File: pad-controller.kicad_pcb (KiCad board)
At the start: 2 copper layers, 86 x 64 mm, 50 parts, among them J4 Conn_01x02, J6 Conn_01x06, M1 Motor_Servo, M2 Motor_Servo, M3 Motor_Servo, M4 Motor_Servo, Q2 FQP30N06L, SW1 SW_Push_Dual, U1 Xbee, U2 TPS56121, U3 LD1117S33TR_SOT223

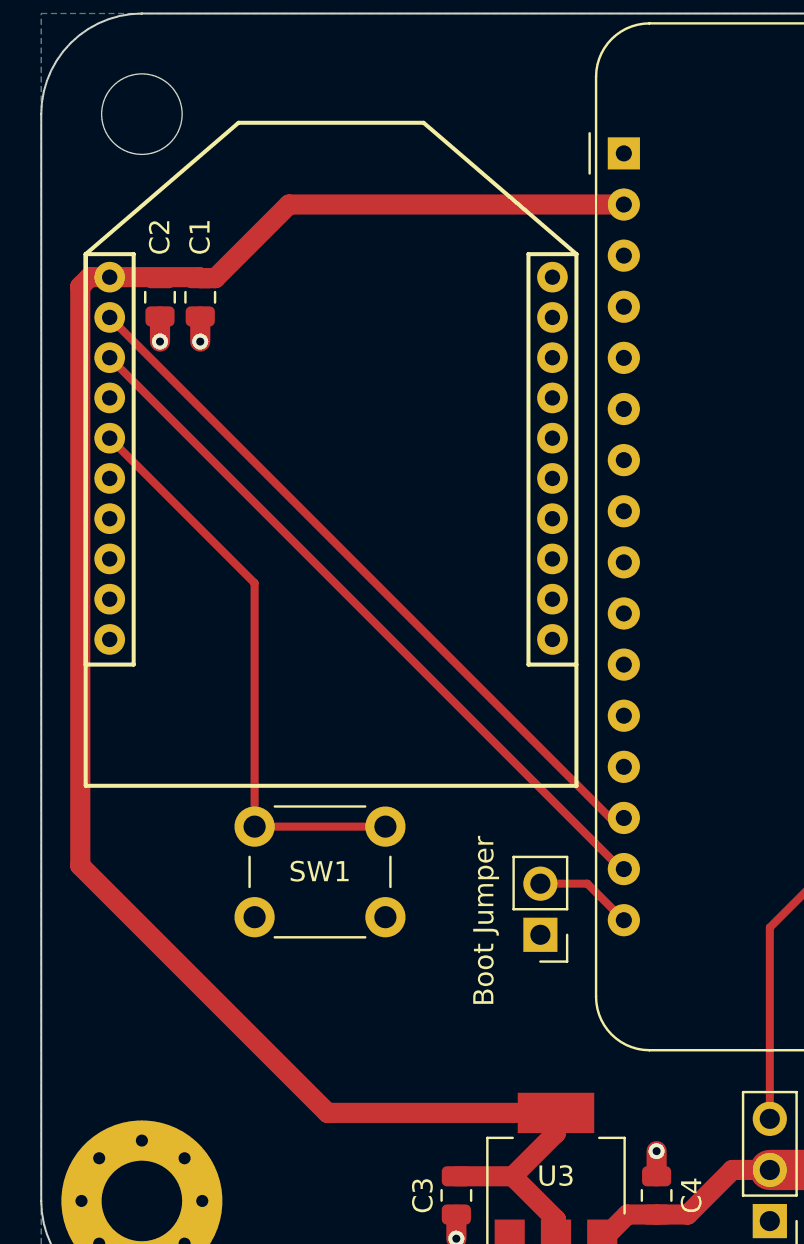
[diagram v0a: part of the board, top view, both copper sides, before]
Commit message: Add HSP logo and 3D model for wago terminal block
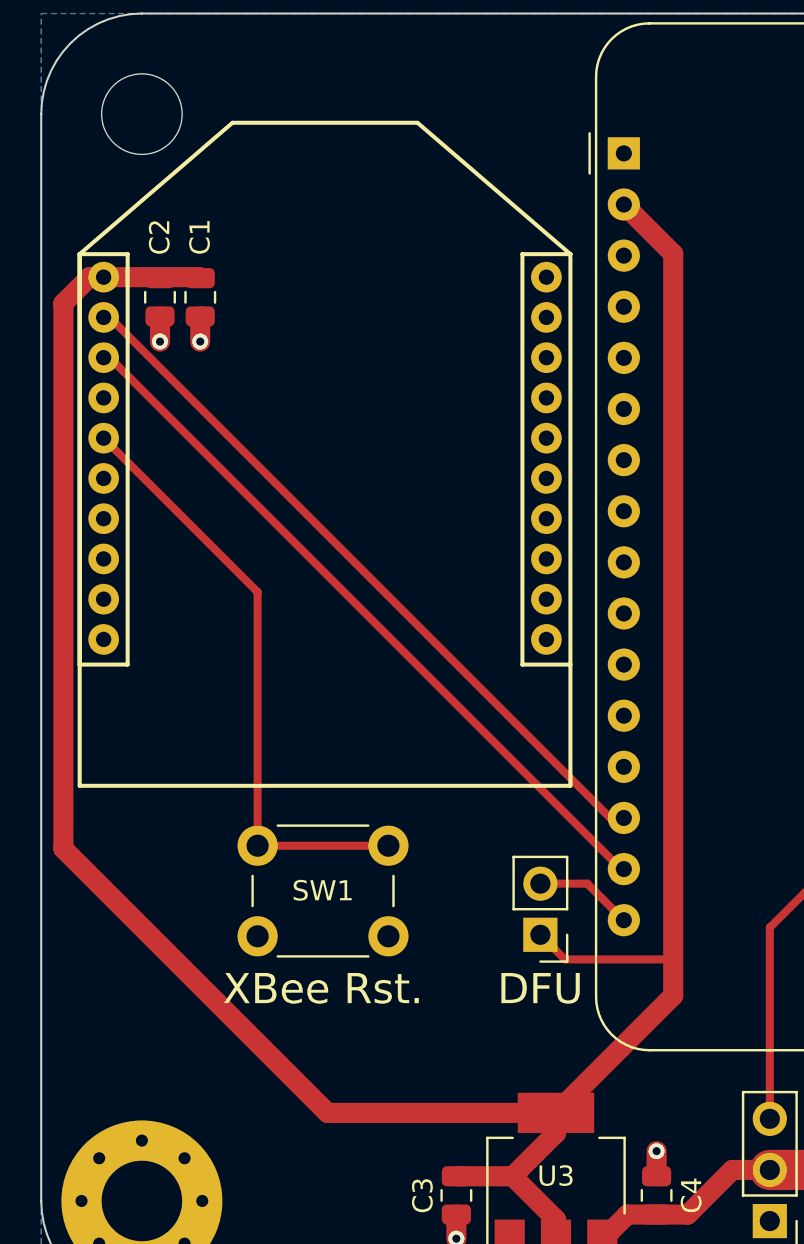
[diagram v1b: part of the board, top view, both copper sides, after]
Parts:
- added G***: LOGO, Logo Footprint Library:hsp-logo, B.Cu at (160.5, 70.7)
- J6: value Conn_01x06 -> Wago Terminal Block
- U1: value Xbee -> XBee
- moved SW1 0.96 mm to (110.8, 101.3)
- moved U1 0.30 mm to (114.1, 82.1)
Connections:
- JP1 pad 1: GND -> +3.3V
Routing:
- net +3.3V: track 97.1 -> 130.9 mm
- net /XBee Reset: track 28.8 -> 29.9 mm
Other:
- board text added: "DFU"
- board text added: "XBee Rst."

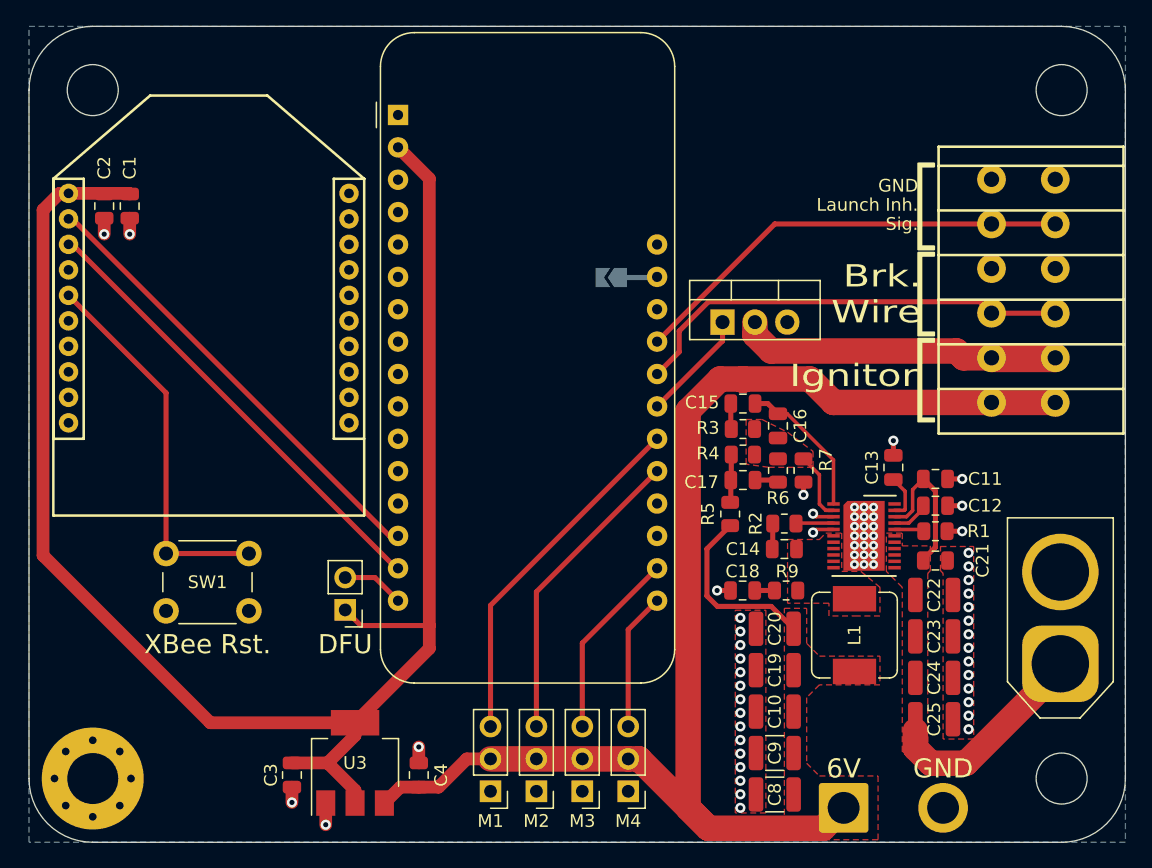
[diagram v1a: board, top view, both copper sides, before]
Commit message: Clean up schematic and board layout
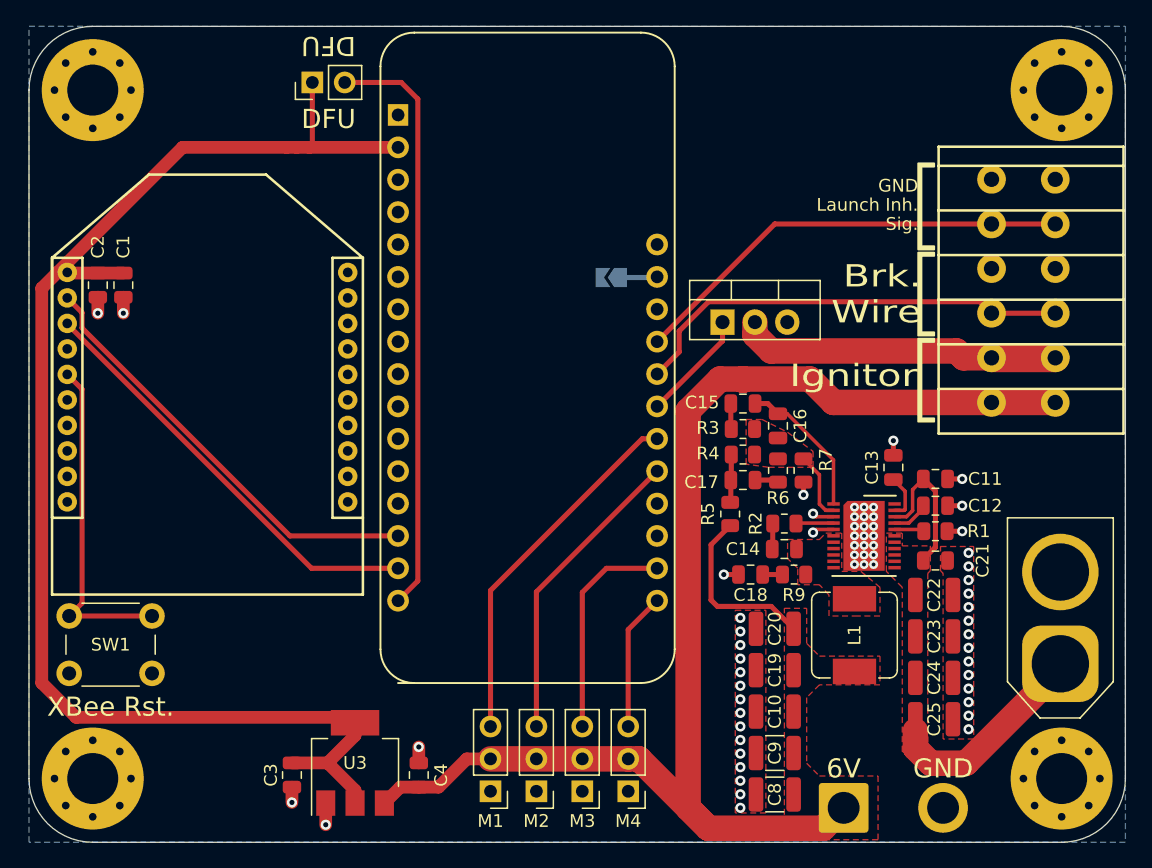
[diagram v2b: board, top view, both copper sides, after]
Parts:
- A1: footprint Module:Adafruit_Feather -> Marks_Footprints:Adafruit_Feather
- C15: value 390 pF -> 56 pF
- C16: value 12 pF -> 1.2 pF
- C17: value 820 pF -> 100 pF
- H1, H3, H4: value MountingHole -> MountingHole_Pad; footprint MountingHole:MountingHole_4mm -> MountingHole:MountingHole_4mm_Pad_Via
- R3: value 442 kΩ -> 390 kΩ
- R4: value 200 kΩ -> 20.5 kΩ
- R6: value 6200 Ω -> 5100 Ω
- R7: value 22 kΩ -> 2.2777778 kΩ
- moved JP1 41.5 mm to (122.2, 64.4), turned to 90 degrees
- moved SW1 9.04 mm to (103.2, 106.2)
- moved C1 6.22 mm to (107.4, 80.3)
- moved C2 6.22 mm to (105.4, 80.3)
- moved U1 6.20 mm to (114.0, 88.3)
- moved C18 1.40 mm to (156.6, 103.0)
- moved R9 1.40 mm to (160.0, 103.0)
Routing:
- net Net-(A1-SPARE): track 4.90 -> 46.3 mm
- net +3.3V: track 130.9 -> 110.6 mm
- net /XBee Reset: track 29.9 -> 26.4 mm
- net MCU TX: track 36.4 -> 33.9 mm
- net Servo 3 PWM: track 14.8 -> 17.2 mm
- net MCU RX: track 36.1 -> 34.4 mm
- net Servo 1 PWM: track 28.0 -> 28.7 mm

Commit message: Adjust back silkscreen
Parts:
- moved G*** 2.60 mm to (163.0, 70.0)
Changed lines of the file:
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@@
   )
   (footprint "Logo Footprint Library:hsp-logo" (layer "B.Cu")
-    (at 160.5 70.7 180)
+    (at 163 70 180)
     (attr board_only exclude_from_pos_files exclude_from_bom)
     (fp_text reference "G***" (at 0 0) (layer "B.SilkS") hide
@@
   )
   (gr_text_box "HSP Pad Controller v1.0"
-    (start 123.65 61.5) (end 156.35 65) (layer "B.SilkS")
+    (start 124.85 61.1) (end 157.55 64.6) (layer "B.SilkS")
       (effects (font (size 1.5 1.5) (thickness 0.25) bold) (justify left top mirror))
   )

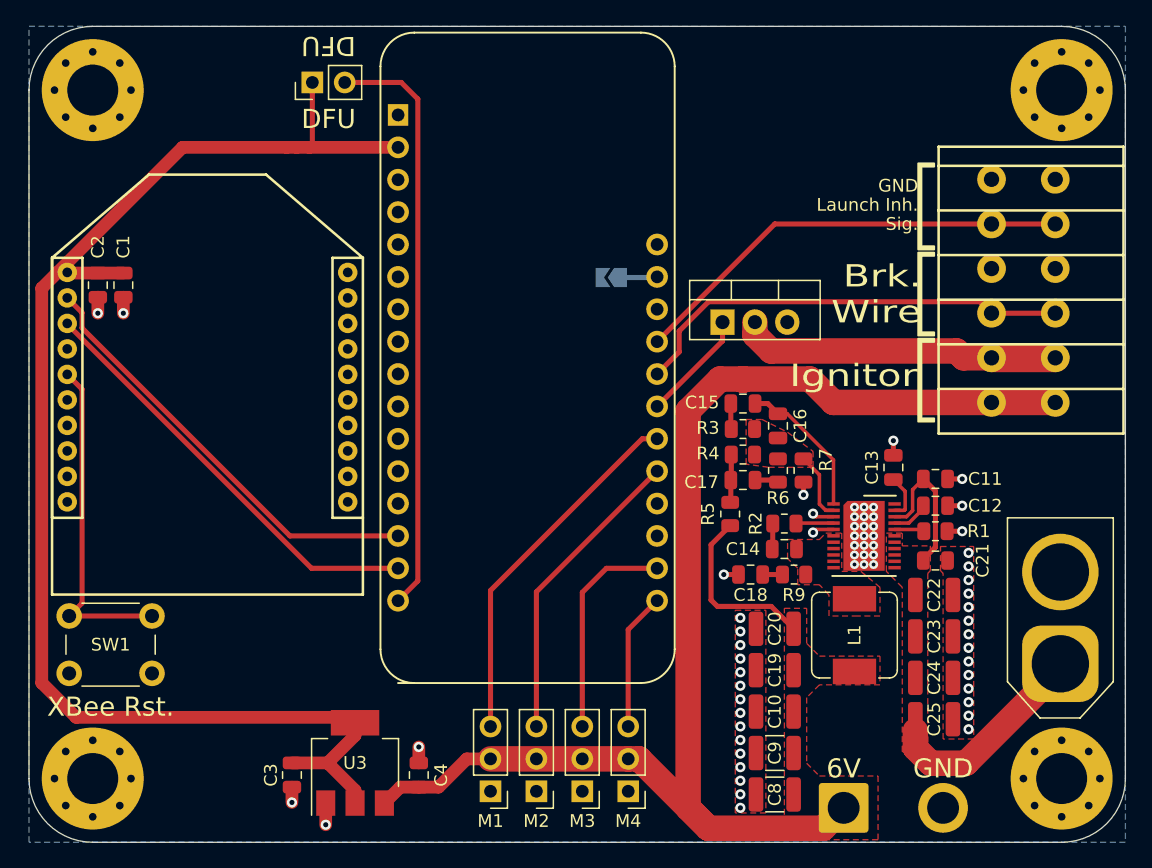
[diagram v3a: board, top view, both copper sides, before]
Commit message: Add silkscreen label for solder jumper
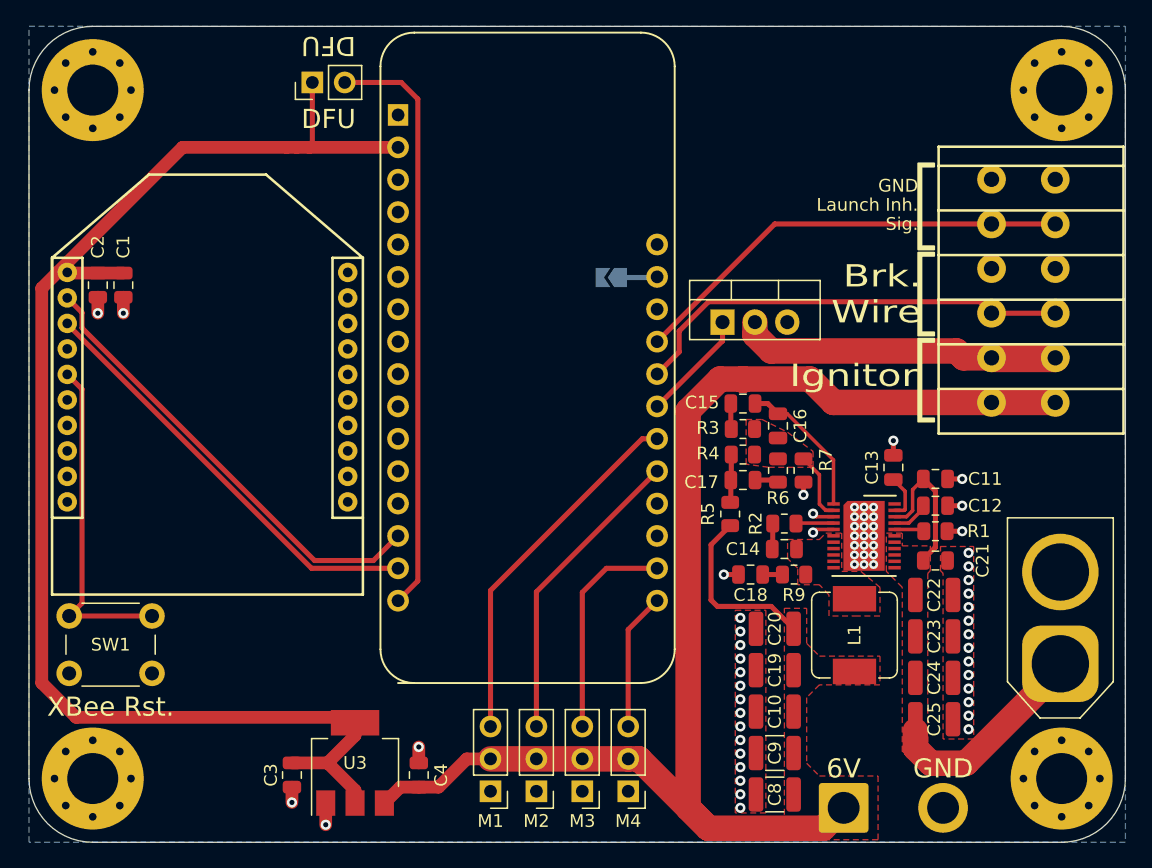
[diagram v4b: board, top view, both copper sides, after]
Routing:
- net MCU RX: track 34.4 -> 36.0 mm
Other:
- board text added: "Feather Regulator Disable"
